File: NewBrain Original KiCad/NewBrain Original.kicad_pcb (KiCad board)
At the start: 2 copper layers, 195 parts, among them J1 Conn_02x03_Top_Bottom, J2 Conn_02x03_Top_Bottom, J3 Conn_02x03_Top_Bottom, J4 Conn_02x03_Top_Bottom, Q1 Q_PNP_EBC, Q100 ZTX107, Q17 ZTX650, Q2 2n5193, Q20 ZTX107, Q49 BC546, Q66 2N3906, Q8 2n5193, U107 IN914, U109 IN914, U401 LM358, U402 74LS153, U403 74LS153, U404 74LS153, U405 74LS153, U406 2764, U407 NEC-PD2364, U408 NEC-PD23128, U409 Z80CPU-DIP, U410 MC1489N, U411 MC1488N, U412 74LS257, U413 74LS174, U414 LM358, U415 HE721A0530, U416 HE751A0510, U417 MC14584BDG, U418 74LS00, U419 COP420L, U420 74LS374, U421 74LS06, U422 74LS161, U423 74LS161, U424 74LS161, U425 74LS74, U426 74LS86, U427 74LS174, U428 74LS257, U429 74LS139, U430 74LS138, U431 74LS32, U432 74LS04, U433 74LS32, U434 74LS86, U435 74LS06, U436 74LS166, U437 74LS08, U438 74LS08, U439 74LS04, U440 74LS02, U441 74LS00, U442 74LS138, U443 74LS11, U444 74LS157_UNITS, U445 74LS112, U446 74LS21, U447 74LS393, U448 74LS10, U449 74LS157, U450 74LS04, U451 SN74LS279AN, U452 MC14584BDG_UNITS, U453 2716-Memory_EPROM, U454 74LS166, U455 74LS27, U456 74LS32, U457 74LS10, U458 74LS90, U459 74LS32, U460 74LS112, U461 74LS95, U462 74LS32, U463 74LS32, U464 74LS11, U465 74LS11, U466 74LS21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

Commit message: Some more link fixes now below 100 warnings.
Signed-off-by: John Bradley <flypie@rocketmail.com>
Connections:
- net /ONE/AB-10 renamed Net-(U453-Pad19)
- net /ONE/AB-7 renamed /ONE/LAB-7
- net /ONE/AB-9 renamed Net-(U453-Pad22)
- net /ONE/DB-0 renamed /ONE/LDB-0
- net /ONE/DB-1 renamed /ONE/LDB-1
- net /ONE/DB-2 renamed /ONE/LDB-2
- net /ONE/DB-3 renamed /ONE/LDB-3
- net /ONE/DB-4 renamed /ONE/LDB-4
- net /ONE/DB-5 renamed /ONE/LDB-5
- net /ONE/DB-6 renamed /ONE/LDB-6
- net /ONE/DB-7 renamed /ONE/LDB-7
- net /ONE/RDDK renamed RDDK
- net /TWO/A15G renamed /TWO/AB-15G
- net /TWO/AD1 renamed AD1
- net /TWO/PRTOV renamed PRTOV
- net /TWO/PWRUP renamed PWRUP
- net /TWO/TPIN renamed TPIN
- net /TWO/TVP renamed TVP
- net /TWO/~A14M renamed /TWO/~AB-14M
- net /TWO/~CLCSA renamed /TWO/~CLUSA
- net /TWO/~CLK renamed ~CLK
- net /TWO/~CLKINT renamed ~CLKINT
- net /TWO/~HALT renamed ~HALT
- net /TWO/~INT renamed ~INT
- net /TWO/~MREQ renamed ~MREQ
- net /TWO/~NMI renamed ~NMI
- net /TWO/~RD renamed ~RD
- net /TWO/~TVTL renamed ~TVTL
- net /TWO/~WAIT renamed ~WAIT
- net /TWO/~WR renamed ~WR
- net Net-(U409-Pad23) renamed ~BUSAK
- C22 pad 2: /TWO/GRND -> GND
- C23 pad 2: /TWO/GRND -> GND
- C94 pad 1: /TWO/~TM1 -> ~TM1
- C95 pad 1: /TWO/~TM2 -> ~TM2
- D1 pad 1: /TWO/GRND -> GND
- D21 pad 2: /TWO/GRND -> GND
- D24 pad 1: /TWO/GRND -> GND
- D31 pad 1: /TWO/GRND -> GND
- D93 pad 2: /TWO/~TM2 -> ~TM2
- D96 pad 2: /TWO/~TM1 -> ~TM1
- PWRIN1 pad 5: /TWO/GRND -> GND
- R114 pad 2: /ONE/TDO -> TDO
- R32 pad 2: /TWO/GRND -> GND
- R33 pad 2: /TWO/GRND -> GND
- R35 pad 2: /TWO/~IOREQ -> ~IOREQ
- R43 pad 2: /TWO/GRND -> GND
- R46 pad 2: /TWO/GRND -> GND
- R50 pad 2: Net-(R50-Pad2) -> ~BUSRQ
- U402 pad 13: Net-(U402-Pad13) -> GND
- U403 pad 6: Net-(U403-Pad6) -> AB-4
- U406 pad 20: Net-(U406-Pad20) -> /TWO/~ROM2
- U406 pad 22: Net-(U406-Pad22) -> /TWO/~ROM2
- U407 pad 20: Net-(U407-Pad20) -> /TWO/~ROM1
- U408 pad 20: Net-(U408-Pad20) -> /TWO/~ROM0
- U409 pad 20: /TWO/~IOREQ -> ~IOREQ
- U409 pad 25: Net-(R50-Pad2) -> ~BUSRQ
- U409 pad 26: /TWO/~RESET -> ~RESET
- U409 pad 27: /TWO/33E -> ~M1
- U409 pad 28: /TWO/~RFSH -> ~RFSH
- U410 pad 11: /ONE/~CTSD -> ~CTSD
- U410 pad 14: Net-(U410-Pad14) -> VCC
- U410 pad 7: Net-(U410-Pad7) -> GND
- U410 pad 8: /ONE/~CTSP -> ~CTSP
- U411 pad 12: /ONE/~RTSD -> ~RTSD
- U411 pad 13: /ONE/~RTSD -> ~RTSD
- U411 pad 14: Net-(U411-Pad14) -> VCC
- U411 pad 7: Net-(U411-Pad7) -> GND
- U411 pad 9: /ONE/PO -> PO
- U412 pad 13: /TWO/~CTSP -> ~CTSP
- U412 pad 6: /TWO/~CTSD -> ~CTSD
- U413 pad 1: /TWO/~RST -> ~RESET
- U413 pad 10: /TWO/~RTSD -> ~RTSD
- U413 pad 12: /TWO/P0 -> PO
- U413 pad 7: /TWO/D0 -> DB-0
- U415 pad 6: /ONE/~TM2 -> ~TM2
- U416 pad 6: /ONE/~TM1 -> ~TM1
- U419 pad 16: /TWO/TDI -> TDI
- U419 pad 27: /TWO/TDO -> TDO
- U419 pad 4: /TWO/~RESET -> ~RESET
- U420 pad 11: /ONE/~TVCLK -> ~TVCLK
- U420 pad 13: /ONE/RD0 -> RD0
- U420 pad 14: /ONE/RD1 -> RD1
- U420 pad 17: /ONE/RD4 -> RD4
- U420 pad 18: /ONE/RD5 -> RD5
- U420 pad 3: /ONE/RD7 -> RD7
- U420 pad 4: /ONE/RD6 -> RD6
- U420 pad 7: /ONE/RD3 -> RD3
- U420 pad 8: /ONE/RD2 -> RD2
- U421 pad 10: Net-(U421-Pad10) -> GND
- U421 pad 11: /TWO/RD0 -> RD0
- U421 pad 12: /TWO/RD1 -> RD1
- U421 pad 13: /TWO/RD2 -> RD2
- U421 pad 14: /TWO/RD3 -> RD3
- U421 pad 15: /TWO/RD4 -> RD4
- U421 pad 16: /TWO/RD5 -> RD5
- U421 pad 17: /TWO/RD6 -> RD6
- U421 pad 18: /TWO/RD7 -> RD7
- U424 pad 15: Net-(U424-Pad15) -> Net-(U422-Pad7)
- U424 pad 16: Net-(U424-Pad16) -> VCC
- U424 pad 4: Net-(U424-Pad4) -> /TWO/80L
- U424 pad 5: Net-(U424-Pad5) -> GND
- U424 pad 6: Net-(U424-Pad6) -> GND
- U424 pad 7: Net-(U424-Pad7) -> VCC
- U424 pad 8: Net-(U424-Pad8) -> GND
- U425 pad 11: /TWO/~TVCLK -> ~TVCLK
- U428 pad 10: /TWO/A15 -> AB-15
- U428 pad 3: /TWO/A13 -> AB-13
- U428 pad 6: /TWO/A14 -> AB-14
- U429 pad 1: /TWO/~EXP2 -> /TWO/~EXP0
- U429 pad 10: /TWO/~COG -> /TWO/~COP
- U429 pad 13: /TWO/AB1 -> AB-1
- U429 pad 14: /TWO/AB0 -> AB-0
- U429 pad 2: /TWO/AB0 -> AB-0
- U429 pad 3: /TWO/AB1 -> AB-1
- U430 pad 1: /TWO/AB2 -> AB-2
- U430 pad 14: /TWO/EXP1 -> /TWO/~EXP1
- U430 pad 15: /TWO/EXP0 -> /TWO/~EXP0
- U430 pad 2: /TWO/AB3 -> AB-3
- U430 pad 3: /TWO/AB4 -> AB-4
- U430 pad 4: /TWO/~IORQ -> ~IOREQ
- U430 pad 6: /TWO/~M1 -> ~M1
- U431 pad 13: /TWO/AB0 -> AB-0
- U432 pad 13: /TWO/1\8 -> 1\8
- U432 pad 2: /TWO/1\8 -> 1\8
- U434 pad 10: /ONE/TDO -> TDO
- U434 pad 8: /ONE/TDI -> TDI
- U435 pad 10: /ONE/~BUSRQ -> ~BUSRQ
- U435 pad 12: (no net) -> Net-(U426-Pad9)
- U435 pad 13: (no net) -> /ONE/RC3
- U436 pad 7: /ONE/~CKVSR -> ~CKVSR
- U437 pad 6: /ONE/AB-8 -> /ONE/LAB-8
- U438 pad 9: /TWO/~TVCLK -> ~TVCLK
- U441 pad 8: /TWO/~CKVSR -> ~CKVSR
- U442 pad 6: /TWO/~RFRSH -> ~RFSH
- U442 pad 8: Net-(U442-Pad8) -> GND
- U447 pad 11: Net-(U447-Pad11) -> Net-(U446-Pad4)
- U450 pad 10: Net-(U426-Pad9) -> (no net)
- U450 pad 11: /ONE/RC3 -> (no net)
- U452 pad 6: /TWO/~RESET -> ~RESET
- U453 pad 18: Net-(U453-Pad18) -> /ONE/UCR
- U453 pad 2: /ONE/AB-6 -> /ONE/LAB-6
- U453 pad 23: /ONE/AB-8 -> Net-(U453-Pad23)
- U453 pad 3: /ONE/AB-5 -> /ONE/LAB-5
- U453 pad 4: /ONE/AB-4 -> /ONE/LAB-4
- U453 pad 5: /ONE/AB-3 -> /ONE/LAB-3
- U453 pad 6: /ONE/AB-2 -> /ONE/LAB-2
- U453 pad 7: /ONE/AB-1 -> /ONE/LAB-1
- U453 pad 8: /ONE/AB-0 -> /ONE/LAB-0
- U454 pad 7: /ONE/~CKVSR -> ~CKVSR
- U455 pad 1: /ONE/AB-5 -> /ONE/LAB-5
- U455 pad 10: /ONE/AB-1 -> /ONE/LAB-1
- U455 pad 11: /ONE/AB-0 -> /ONE/LAB-0
- U455 pad 13: /ONE/AB-6 -> /ONE/LAB-6
- U455 pad 4: /ONE/AB-4 -> /ONE/LAB-4
- U455 pad 5: /ONE/AB-3 -> /ONE/LAB-3
- U455 pad 9: /ONE/AB-2 -> /ONE/LAB-2
- U456 pad 3: /ONE/AB-8 -> Net-(U453-Pad23)
- U458 pad 10: Net-(U458-Pad10) -> GND
- U458 pad 5: Net-(U458-Pad5) -> VCC
- U460 pad 15: Net-(U460-Pad15) -> VCC
- U460 pad 4: Net-(U460-Pad4) -> VCC
- U465 pad 9: /TWO/~RFRSH -> ~RFSH
- U468 pad 1: /ONE/1\8 -> 1\8

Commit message: Resolve inconsistencies in circuit diagram buy following traces.
Resistor name used twice temp solution add a and b to name.

Signed-off-by: John Bradley <flypie@rocketmail.com>
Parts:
- removed the R25 at (178.4, 53.8)
- removed R26, R54: 4K7, Resistor_THT:R_Axial_DIN0204_L3.6mm_D1.6mm_P1.90mm_Vertical
- removed R34, R35, R37, R38, R47, R48, R49: 4k7, Resistor_THT:R_Axial_DIN0204_L3.6mm_D1.6mm_P1.90mm_Vertical
- removed R61: 22k, Resistor_THT:R_Axial_DIN0204_L3.6mm_D1.6mm_P1.90mm_Vertical
- added J1: Conn_01x10, Connector_JST:JST_EH_B10B-EH-A_1x10_P2.50mm_Vertical, F.Cu at (295.9, 90.2)
- added J2: Conn_01x10, Connector_JST:JST_EH_B10B-EH-A_1x10_P2.50mm_Vertical, F.Cu at (325.5, 90.2)
- added J21: Conn_02x25_Top_Bottom, Connector_PinHeader_2.54mm:PinHeader_2x25_P2.54mm_Vertical, F.Cu at (287.5, 84.8)
- added J3: Conn_01x10, Connector_JST:JST_EH_B10B-EH-A_1x10_P2.50mm_Vertical, F.Cu at (295.9, 100.5)
- added J31: Conn_01x12_Top_Bottom, Connector_JST:JST_EH_B12B-EH-A_1x12_P2.50mm_Vertical, F.Cu at (298.4, 115.6)
- added J4: Conn_01x10, Connector_JST:JST_EH_B10B-EH-A_1x10_P2.50mm_Vertical, F.Cu at (325.5, 100.5)
- added RN54: 4K7, Resistor_THT:R_Array_SIP9, F.Cu at (301.8, 105.4)
- added RN59: R_Network08, Resistor_THT:R_Array_SIP9, F.Cu at (326.6, 105.4)
- added RN66: R_Network03, Resistor_THT:R_Array_SIP5, F.Cu at (287.4, 155.1)
- C12: renamed from C16; value 33pf -> 680pf
- C18: value 0.1 -> 0.1uf
- C19: renamed from C11; value 33pf -> 0.1uf
- C23: renamed from C20; value 33pf -> 0.1uf
- C26: renamed from C12; value 33pf -> 0.1uf
- C29: renamed from C14; value 33pf -> 0.1uf
- C33: renamed from C13; value CP -> 47uf
- C5: renamed from C15; value 33pf -> 680pf
- C51: renamed from C17; value 33pf -> 27pF
- C55: renamed from C19; value 33pf -> 100pf
- C6: renamed from C23; value CP -> 22 uF
- C7: renamed from C22; value CP -> 47uf
- C9: renamed from C21; value 33pf -> 0.1uf
- Q110: renamed from Q1; value Q_PNP_EBC -> ZTC212
- R10: renamed from R29; value 22 -> 4K7
- R14: renamed from R42; value 22 -> 41k2
- R15: renamed from R43; value 22 -> 39K
- R16: renamed from R32; value 22 -> 4K7
- R25: renamed from R39; value 22 -> 1.2k
- R28a1: renamed from R27; value 22 -> 28
- R3: renamed from R44; value 22 -> 150k
- R50: value 4k7 -> 33pf; footprint Resistor_THT:R_Axial_DIN0204_L3.6mm_D1.6mm_P1.90mm_Vertical -> Capacitor_THT:C_Disc_D3.0mm_W1.6mm_P2.50mm
- R81: renamed from R22; value R -> 3.3
- moved U401 157.5 mm to (327.0, 141.0)
- moved R50 147.2 mm to (301.2, 109.1)
- renumbered J1 to J11, J2 to J12, J3 to J13, J4 to J14, Q8 to Q22, Q2 to Q8, R31 to R11, R33 to R13, R28 to R27, R23 to R28b1, R46 to R4, R41 to R43, R36 to R52, R13 to R71
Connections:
- net /ONE/1\2 renamed 1\2
- net /ONE/1\4 renamed 1\4
- net /ONE/FRM renamed FRM
- net /ONE/K11 renamed K11
- net /ONE/LLVD renamed LLVD
- net /ONE/TVSD renamed TVSD
- net /TWO/CIA renamed /TWO/~ACIA
- net ~CLK renamed /TWO/~CLK
- net ~RFSH renamed /TWO/~RFSH
- C104 pad 1: GND -> K12
- C119 pad 1: GND -> K12
- C120 pad 1: GND -> K12
- C132 pad 2: GND -> K12
- C133 pad 1: GND -> K12
- C18 pad 1: GND -> K12
- C18 pad 2: /TWO/+12I -> -12I
- C19 pad 1: GND -> K12
- C23 pad 2: /TWO/+5 -> VCC
- C26 pad 1: GND -> K12
- C29 pad 1: GND -> K12
- C29 pad 2: Net-(C13-Pad1) -> V0A
- C33 pad 1: Net-(C13-Pad1) -> V0A
- C33 pad 2: GND -> K12
- C44 pad 1: GND -> K12
- C55 pad 1: GND -> K12
- C6 pad 1: /TWO/+12 -> +12
- C6 pad 2: GND -> K12
- C64 pad 1: Net-(C64-Pad1) -> /TWO/1\8c
- C7 pad 1: /TWO/+5 -> VCC
- C7 pad 2: GND -> K12
- C72 pad 2: GND -> K12
- C73 pad 1: GND -> K12
- C9 pad 2: /TWO/+12 -> +12
- C94 pad 2: GND -> K12
- C95 pad 2: GND -> K12
- D1 pad 1: GND -> K12
- D21 pad 2: GND -> K12
- D24 pad 1: GND -> K12
- D31 pad 1: GND -> K12
- J11 pad 6: GND -> K12
- J12 pad 1: Net-(J2-Pad1) -> Net-(J12-Pad1)
- J12 pad 6: GND -> K12
- J13 pad 6: GND -> K12
- J14 pad 6: GND -> K12
- PWRIN1 pad 3: /TWO/-12I -> -12I
- PWRIN1 pad 5: GND -> K12
- PWRIN1 pad 6: VCC -> /TWO/+5I
- Q100 pad 1: GND -> K12
- Q22 pad 1: /TWO/+5 -> /TWO/+5I
- Q22 pad 2: /TWO/+5I -> VCC
- Q8 pad 1: /TWO/+12 -> /TWO/+12I
- Q8 pad 2: /TWO/+12I -> +12
- R106 pad 1: GND -> K12
- R123 pad 1: GND -> K12
- R128 pad 1: GND -> K12
- R129 pad 1: GND -> K12
- R13 pad 2: GND -> K12
- R14 pad 1: /TWO/+5 -> VCC
- R15 pad 2: GND -> K12
- R16 pad 2: GND -> K12
- R2 pad 1: /TWO/+12I -> -12I
- R28a1 pad 2: Net-(C13-Pad1) -> V0A
- R28b1 pad 2: /TWO/RAMINH -> /TWO/RMSL
- R3 pad 1: /TWO/+12 -> +12
- R4 pad 2: GND -> K12
- R43 pad 2: GND -> K12
- R50 pad 1: VCC -> K12
- R50 pad 2: ~BUSRQ -> Net-(Q49-Pad1)
- R60 pad 1: GND -> K12
- R62 pad 1: Net-(C64-Pad1) -> /TWO/1\8c
- R77 pad 1: GND -> K12
- R79 pad 1: GND -> K12
- R97 pad 1: GND -> K12
- U109 pad 1: GND -> K12
- U401 pad 4: Net-(U401-Pad4) -> K12
- U401 pad 8: VCC -> V0A
- U402 pad 1: GND -> K12
- U402 pad 12: GND -> Net-(U402-Pad12)
- U402 pad 13: GND -> Net-(U402-Pad12)
- U402 pad 15: GND -> K12
- U402 pad 8: GND -> K12
- U403 pad 1: GND -> K12
- U403 pad 15: GND -> K12
- U403 pad 8: GND -> K12
- U404 pad 1: GND -> K12
- U404 pad 15: GND -> K12
- U404 pad 8: GND -> K12
- U405 pad 1: GND -> K12
- U405 pad 15: GND -> K12
- U405 pad 8: GND -> K12
- U406 pad 14: GND -> K12
- U407 pad 12: GND -> K12
- U408 pad 14: GND -> K12
- U408 pad 22: Net-(U408-Pad22) -> /TWO/~ROM0
- U409 pad 17: ~NMI -> /TWO/~NMI
- U409 pad 18: ~HALT -> /TWO/~HALT
- U409 pad 23: ~BUSAK -> /TWO/~BUSAK
- U409 pad 24: ~WAIT -> /TWO/~WAIT
- U409 pad 29: GND -> K12
- U410 pad 1: Net-(J2-Pad1) -> Net-(J12-Pad1)
- U410 pad 12: Net-(J2-Pad1) -> Net-(RN66-Pad3)
- U410 pad 2: Net-(J2-Pad1) -> Net-(RN66-Pad2)
- U410 pad 7: GND -> K12
- U410 pad 9: Net-(J2-Pad1) -> Net-(RN66-Pad4)
- U411 pad 1: Net-(U411-Pad1) -> -12I
- U411 pad 14: VCC -> +12
- U411 pad 4: /ONE/DO -> DO
- U411 pad 5: /ONE/DO -> DO
- U411 pad 7: GND -> K12
- U412 pad 1: AD1 -> AB-1
- U412 pad 3: /TWO/~COPINT -> RDDK
- U412 pad 8: GND -> K12
- U413 pad 7: DB-0 -> DO
- U413 pad 8: GND -> K12
- U414 pad 4: /ONE/V0 -> K12
- U414 pad 8: GND -> V0A
- U415 pad 9: GND -> K12
- U417 pad 7: Net-(U417-Pad7) -> K12
- U417 pad 8: /ONE/TPIN -> TPIN
- U418 pad 7: Net-(U417-Pad7) -> K12
- U419 pad 1: GND -> K12
- U420 pad 1: GND -> K12
- U420 pad 10: GND -> K12
- U420 pad 12: /ONE/AB-0 -> /ONE/LAB-0
- U420 pad 15: /ONE/AB-1 -> /ONE/LAB-1
- U420 pad 16: /ONE/AB-4 -> /ONE/LAB-4
- U420 pad 19: /ONE/AB-5 -> /ONE/LAB-5
- U420 pad 5: /ONE/AB-6 -> /ONE/LAB-6
- U420 pad 6: /ONE/AB-3 -> /ONE/LAB-3
- U420 pad 9: /ONE/AB-2 -> /ONE/LAB-2
- U421 pad 10: GND -> K12
- U422 pad 1: Net-(U422-Pad1) -> ~FRMR
- U422 pad 11: GND -> Net-(U402-Pad12)
- U422 pad 16: GND -> K12
- U422 pad 8: GND -> K12
- U423 pad 1: Net-(U422-Pad1) -> ~FRMR
- U423 pad 16: GND -> K12
- U423 pad 8: GND -> K12
- U424 pad 1: /TWO/~FRMR -> ~FRMR
- U424 pad 10: Net-(U424-Pad10) -> Net-(U405-Pad4)
- U424 pad 2: Net-(U424-Pad2) -> Net-(U422-Pad2)
- U424 pad 4: /TWO/80L -> 80L
- U424 pad 5: GND -> K12
- U424 pad 6: GND -> K12
- U424 pad 8: GND -> K12
- U425 pad 10: Net-(U425-Pad10) -> VCC
- U425 pad 7: Net-(U417-Pad7) -> K12
- U425 pad 9: Net-(U424-Pad10) -> Net-(U405-Pad4)
- U426 pad 10: /ONE/CRDO -> /ONE/LDB-0
- U426 pad 12: /ONE/RV -> RV
- U426 pad 5: /TWO/RAMINH -> /TWO/RMSL
- U426 pad 6: /TWO/~AB-14M -> /TWO/~A14M
- U426 pad 7: GND -> K12
- U427 pad 10: /TWO/~32\40 -> /TWO/32\40
- U427 pad 12: /TWO/F5 -> FS
- U427 pad 15: /TWO/RV -> RV
- U427 pad 2: /TWO/UCR -> UCR
- U427 pad 5: /TWO/~ENRG -> Net-(U427-Pad5)
- U427 pad 7: /TWO/80L -> 80L
- U427 pad 8: GND -> K12
- U428 pad 8: GND -> K12
- U429 pad 12: /TWO/~CLCLK -> ~CLCLK
- U429 pad 8: Net-(U417-Pad7) -> K12
- U429 pad 9: /TWO/~ENRG1 -> /TWO/~ENRG
- U430 pad 10: /TWO/~VST -> /TWO/~UST
- U430 pad 12: ~TVTL -> /TWO/~TVCTL
- U430 pad 5: PRTOV -> /TWO/PRTOV
- U430 pad 8: GND -> K12
- U431 pad 7: Net-(U401-Pad4) -> K12
- U432 pad 7: Net-(U401-Pad4) -> K12
- U432 pad 9: Net-(C64-Pad1) -> /TWO/1\8c
- U433 pad 12: /ONE/UCR -> UCR
- U433 pad 7: Net-(U417-Pad7) -> K12
- U434 pad 7: Net-(U401-Pad4) -> K12
- U434 pad 9: /ONE/TPIN -> TPIN
- U435 pad 13: /ONE/RC3 -> RC3
- U435 pad 7: Net-(U417-Pad7) -> K12
- U436 pad 1: GND -> K12
- U436 pad 6: GND -> K12
- U436 pad 8: GND -> K12
- U436 pad 9: /ONE/~GR -> ~GR
- U437 pad 1: /ONE/RC3 -> RC3
- U437 pad 5: /ONE/FS -> FS
- U437 pad 6: /ONE/LAB-8 -> /ONE/LAB-7
- U437 pad 7: GND -> K12
- U438 pad 1: /ONE/UCR -> UCR
- U438 pad 2: /ONE/RC3 -> RC3
- U438 pad 7: Net-(U417-Pad7) -> K12
- U438 pad 8: Net-(U424-Pad2) -> Net-(U422-Pad2)
- U439 pad 1: /TWO/80L -> 80L
- U439 pad 11: /ONE/FS -> FS
- U439 pad 7: Net-(U417-Pad7) -> K12
- U440 pad 12: /ONE/~VDLD -> ~VDLD
- U440 pad 4: Net-(U440-Pad4) -> GR
- U440 pad 5: Net-(U440-Pad5) -> ~GR
- U440 pad 6: Net-(U440-Pad5) -> ~GR
- U440 pad 7: GND -> K12
- U441 pad 11: Net-(U439-Pad3) -> Net-(U441-Pad11)
- U441 pad 6: /TWO/~VDLD -> ~VDLD
- U441 pad 7: Net-(U417-Pad7) -> K12
- U442 pad 8: GND -> K12
- U443 pad 10: /TWO/RC2 -> RC2
- U443 pad 11: /TWO/RC1 -> RC1
- U443 pad 6: Net-(U403-Pad4) -> Net-(U443-Pad6)
- U443 pad 7: Net-(U417-Pad7) -> K12
- U443 pad 9: /TWO/UCR -> UCR
- U444 pad 1: /TWO/80L -> 80L
- U444 pad 10: Net-(U403-Pad4) -> Net-(U443-Pad6)
- U444 pad 15: GND -> K12
- U444 pad 2: Net-(U403-Pad4) -> Net-(U443-Pad6)
- U444 pad 6: Net-(U439-Pad3) -> Net-(U441-Pad11)
- U444 pad 8: GND -> K12
- U445 pad 14: /TWO/~FRMR -> ~FRMR
- U445 pad 15: /TWO/~FRMR -> ~FRMR
- U445 pad 8: GND -> K12
- U446 pad 1: /ONE/GR -> GR
- U446 pad 12: /ONE/FP -> FP
- U446 pad 2: /ONE/32\40 -> /TWO/32\40
- U446 pad 7: Net-(U417-Pad7) -> K12
- U447 pad 1: Net-(U447-Pad1) -> RC0
- U447 pad 5: Net-(U446-Pad5) -> Net-(U447-Pad5)
- U447 pad 7: Net-(U401-Pad4) -> K12
- U448 pad 13: Net-(U446-Pad5) -> Net-(U447-Pad5)
- U448 pad 7: GND -> K12
- U449 pad 15: GND -> K12
- U449 pad 8: GND -> K12
- U450 pad 2: /ONE/~FRMR -> ~FRMR
- U450 pad 7: Net-(U417-Pad7) -> K12
- U451 pad 11: /ONE/FPO -> FP
- U451 pad 13: /ONE/~CLKINT -> ~CLKINT
- U451 pad 14: /ONE/~FRMR -> ~FRMR
- U451 pad 15: /ONE/~CLCLK -> ~CLCLK
- U451 pad 8: GND -> K12
- U451 pad 9: /ONE/~TVS -> ~TVS
- U452 pad 7: Net-(U417-Pad7) -> K12
- U453 pad 12: GND -> K12
- U453 pad 18: /ONE/UCR -> UCR
- U453 pad 20: GND -> K12
- U454 pad 1: GND -> K12
- U454 pad 10: /ONE/AB-3 -> /ONE/LAB-3
- U454 pad 11: /ONE/AB-2 -> /ONE/LAB-2
- U454 pad 12: /ONE/AB-1 -> /ONE/LAB-1
- U454 pad 14: /ONE/AB-0 -> /ONE/LAB-0
- U454 pad 3: /ONE/AB-6 -> /ONE/LAB-6
- U454 pad 4: /ONE/AB-5 -> /ONE/LAB-5
- U454 pad 5: /ONE/AB-4 -> /ONE/LAB-4
- U454 pad 6: GND -> K12
- U454 pad 8: GND -> K12
- U454 pad 9: /ONE/GR -> GR
- U455 pad 7: GND -> K12
- U456 pad 1: /ONE/RC0 -> RC0
- U456 pad 12: /ONE/RC1 -> RC1
- U456 pad 5: /ONE/UCR -> UCR
- U456 pad 7: GND -> K12
- U456 pad 9: /ONE/RC2 -> RC2
- U457 pad 3: Net-(U457-Pad3) -> 1\8
- U457 pad 7: GND -> K12
- U458 pad 1: Net-(U447-Pad1) -> RC0
- U458 pad 10: GND -> K12
- U458 pad 11: /ONE/RC3 -> RC3
- U458 pad 12: /ONE/RC0 -> RC0
- U458 pad 6: GND -> K12
- U458 pad 7: GND -> K12
- U458 pad 8: /ONE/RC2 -> RC2
- U458 pad 9: /ONE/RC1 -> RC1
- U459 pad 1: /TWO/1\16 -> /TWO/~1\16
- U459 pad 10: /ONE/GR -> GR
- U459 pad 4: /ONE/BOL -> 80L
- U459 pad 7: Net-(U417-Pad7) -> K12
- U460 pad 1: Net-(U439-Pad3) -> Net-(U441-Pad11)
- U460 pad 14: /ONE/~GR -> ~GR
- U460 pad 8: Net-(U401-Pad4) -> K12
- U461 pad 2: Net-(U440-Pad5) -> ~GR
- U461 pad 7: GND -> K12
- U462 pad 1: /TWO/GO -> GR
- U462 pad 10: /TWO/RC3 -> RC3
- U462 pad 2: /TWO/RCO -> RC0
- U462 pad 4: /TWO/GO -> GR
- U462 pad 7: GND -> K12
- U463 pad 1: Net-(U440-Pad4) -> GR
- U463 pad 11: Net-(U440-Pad5) -> ~GR
- U463 pad 4: Net-(U463-Pad4) -> Net-(U450-Pad5)
- U463 pad 7: GND -> K12
- U464 pad 7: GND -> K12
- U465 pad 7: GND -> K12
- U466 pad 13: Net-(U446-Pad5) -> Net-(U447-Pad5)
- U466 pad 7: GND -> K12
- U467 pad 7: Net-(U417-Pad7) -> K12
- U468 pad 12: GND -> K12
- U468 pad 2: GND -> K12
- U468 pad 7: GND -> K12
- U469 pad 7: GND -> K12
- U470 pad 4: Net-(U447-Pad1) -> RC0
- U470 pad 7: Net-(U417-Pad7) -> K12
- U471 pad 12: /ONE/FPO -> FP
- U471 pad 2: /ONE/TVP -> TVP
- U471 pad 3: /ONE/TVP -> TVP
- U471 pad 6: /ONE/CSYNC -> CSYNC
- U471 pad 7: Net-(U417-Pad7) -> K12

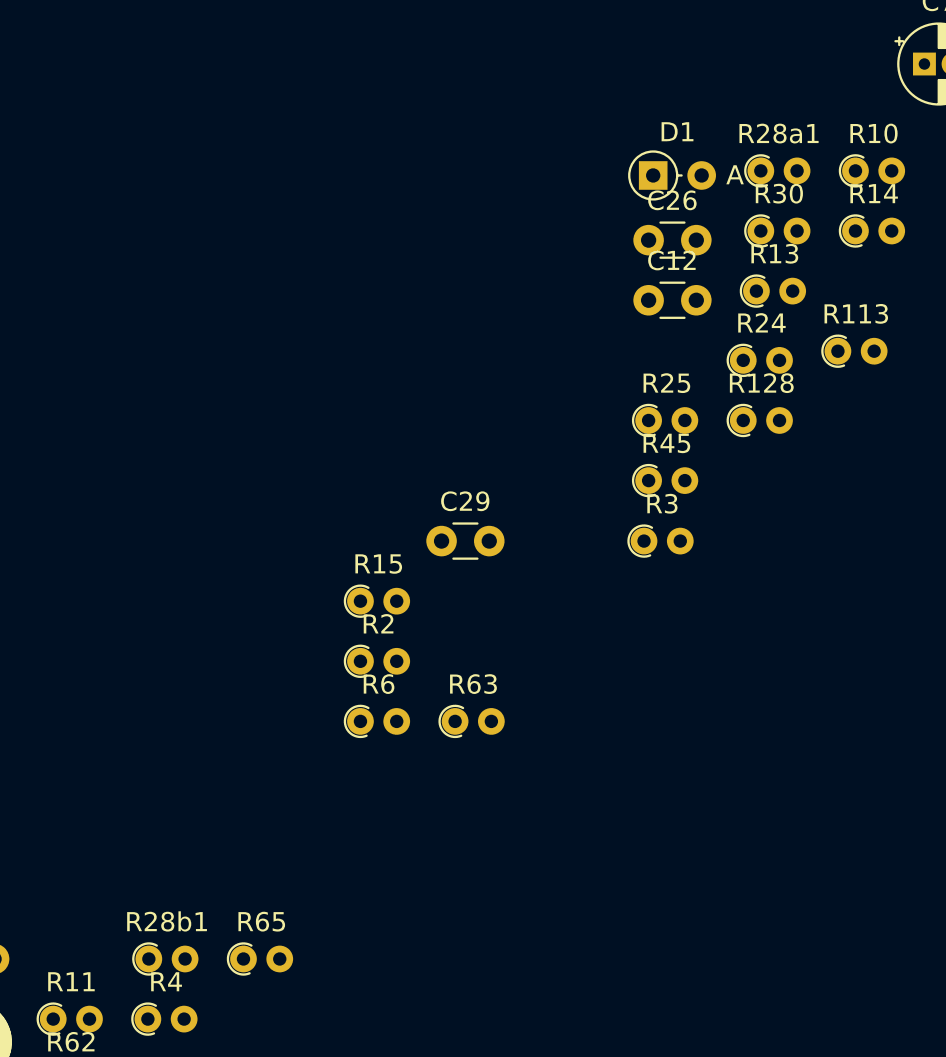
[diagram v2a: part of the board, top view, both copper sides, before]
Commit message: Resolve diplicate R28 from drawings, one is R30 a pullup resistor connected.
Trace 4 pins on memory board header.

Add aligned PCB igmes with alpha channel and beginings of annotated image.


Signed-off-by: John Bradley <flypie@rocketmail.com>
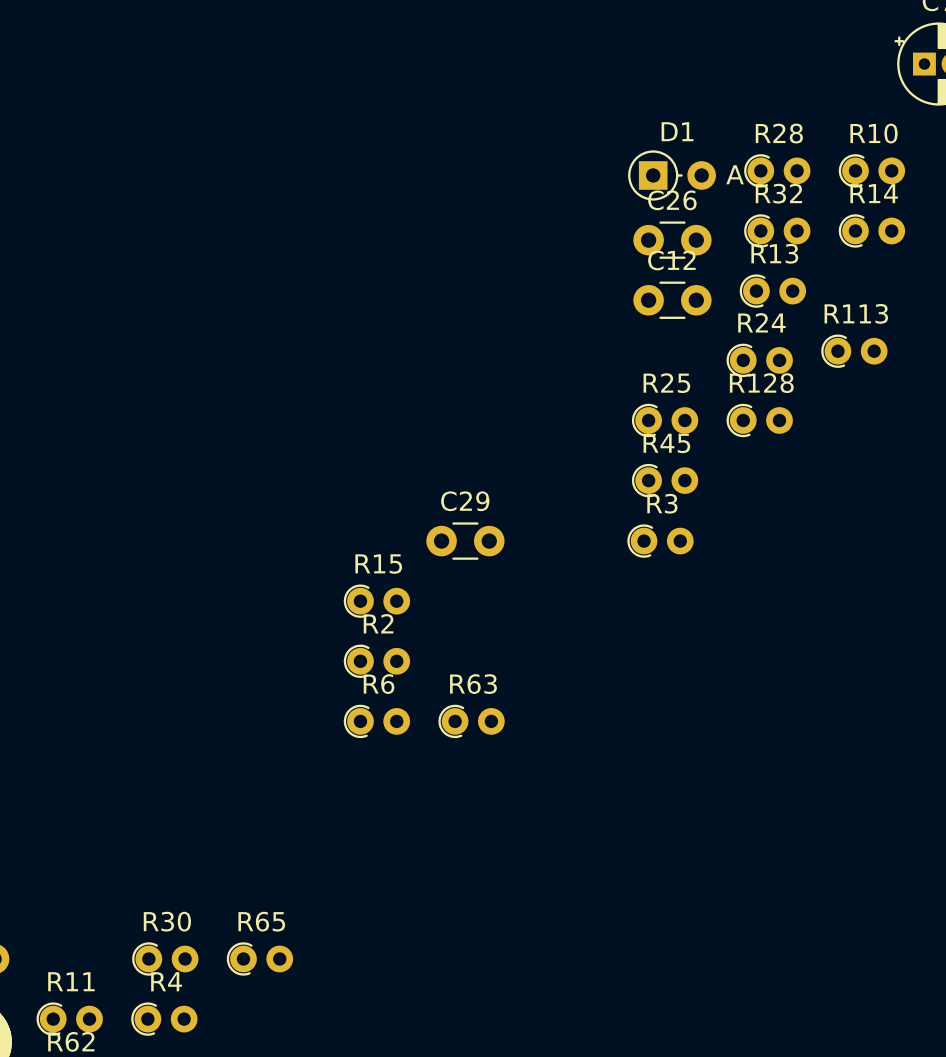
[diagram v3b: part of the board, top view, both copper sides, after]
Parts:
- R27: value 22 -> 4k7
- R28: renamed from R28a1; value 28 -> 100
- R30: renamed from R28b1; value 1K -> 4K7
- R32: renamed from R30; value 32 -> 56
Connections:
- J3 pad 10: /TWO/3.10M -> /TWO/-5v
- J3 pad 7: /TWO/3.7M -> K12
- J3 pad 8: /TWO/3.8M -> VCC
- J3 pad 9: /TWO/3.9M -> K12
